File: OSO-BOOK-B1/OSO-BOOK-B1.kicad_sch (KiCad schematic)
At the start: 72 parts, among them J1 USB_C_Receptacle_USB2.0, J2 Conn_01x02_MountingPin, J3 Conn_01x24, J4 Conn_01x06, J5 JST-PH3, J6 JST-PH4, J7 JST-PH3, J8 Conn_ARM_JTAG_SWD_10, Q1 DMG3415, Q2 Q_PMOS_GSD, Q3 Q_NMOS_GSD, U1 XC6220B331MR-G, U2 ESP32-S3-WROOM-1, U3 MEM2075, U4 MCP73831-2-OT, U5 R1218, Y1 32.768 kHz

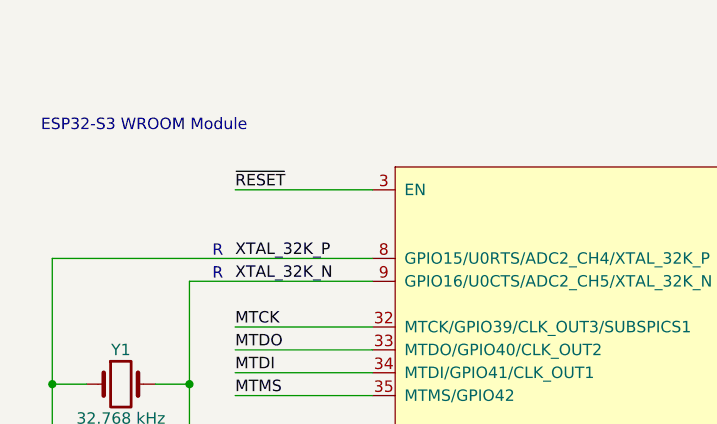
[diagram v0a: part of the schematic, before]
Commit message: add EN pullup to ESP32-S3 book
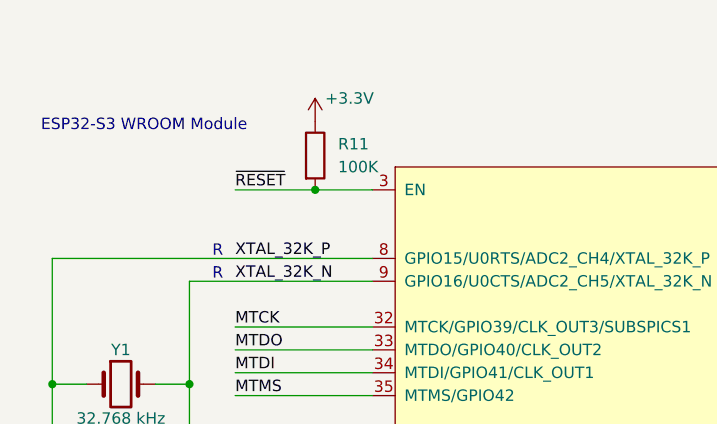
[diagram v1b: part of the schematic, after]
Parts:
- added R11: 100K, Resistor_SMD:R_0805_2012Metric, symbol Device:R
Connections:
- net +3V3: now also R11.1
- net ~{RESET}: now also R11.2
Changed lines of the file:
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@@
   (junction (at 16.51 45.72) (diameter 0) (color 0 0 0 0)
+  )
+  (junction (at 45.72 24.13) (diameter 0) (color 0 0 0 0)
   )
   (junction (at 232.41 149.86) (diameter 0) (color 0 0 0 0)
@@
     (stroke (width 0) (type solid) (color 132 0 0 1))
   )
+  (wire (pts (xy 45.72 24.13) (xy 36.83 24.13))
+    (stroke (width 0) (type default))
+  )
   (wire (pts (xy 44.45 80.01) (xy 36.83 80.01))
     (stroke (width 0) (type default))
@@
     (stroke (width 0) (type default))
   )
-  (wire (pts (xy 52.07 24.13) (xy 36.83 24.13))
+  (wire (pts (xy 52.07 24.13) (xy 45.72 24.13))
     (stroke (width 0) (type default))
   )
@@
     )
   )
+  (symbol (lib_id "Device:R") (at 45.72 20.32 0) (unit 1)
+    (in_bom yes) (on_board yes) (dnp no) (fields_autoplaced)
+    (property "Reference" "R11" (at 48.26 19.0499 0)
+      (effects (font (size 1.27 1.27)) (justify left))
+    )
+    (property "Value" "100K" (at 48.26 21.5899 0)
+      (effects (font (size 1.27 1.27)) (justify left))
+    )
+    (property "Footprint" "Resistor_SMD:R_0805_2012Metric" (at 43.942 20.32 90)
+      (effects (font (size 1.27 1.27)) hide)
+    )
+    (property "Datasheet" "~" (at 45.72 20.32 0)
+      (effects (font (size 1.27 1.27)) hide)
+    )
+    (pin "1")
+    (pin "2")
+    (instances
+      (project "OSO-BOOK-B1"
+        (path "/0e7808ef-4104-4c3a-9f13-425856a8989a"
+          (reference "R11") (unit 1)
+        )
+      )
+      (project "OSO-FLOE-A1"
+        (path "/8cfc6a4c-22f6-4063-b0c4-51ca52a3a57c"
+          (reference "R3") (unit 1)
+        )
+      )
+      (project "OSO-DIGA-A1"
+        (path "/bb4f0314-c44c-4dda-b85c-537120eaae9a"
+          (reference "R4") (unit 1)
+        )
+      )
+    )
+  )
   (symbol (lib_id "Mechanical:Fiducial") (at 262.89 177.8 0) (unit 1)
     (in_bom yes) (on_board yes) (dnp no) (fields_autoplaced)
@@
         )
       )
+    )
+  )
+  (symbol (lib_id "power:+3.3V") (at 45.72 16.51 0) (unit 1)
+    (in_bom yes) (on_board yes) (dnp no)
+    (property "Reference" "#PWR036" (at 45.72 20.32 0)
+      (effects (font (size 1.27 1.27)) hide)
+    )
+    (property "Value" "+3.3V" (at 49.53 13.97 0)
+      (effects (font (size 1.27 1.27)))
+    )
+    (property "Footprint" "" (at 45.72 16.51 0)
+      (effects (font (size 1.27 1.27)) hide)
+    )
+    (property "Datasheet" "" (at 45.72 16.51 0)
+      (effects (font (size 1.27 1.27)) hide)
+    )
+    (pin "1")
+    (instances
+      (project "OSO-BOOK-B1"
+        (path "/0e7808ef-4104-4c3a-9f13-425856a8989a"
+          (reference "#PWR036") (unit 1)
+        )
+      )

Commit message: cleaning up Open Book for Hackaday submission
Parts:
- C19, J4, L2, R8, U5: now not fitted
- C6, C7: value TBD -> 22pF
- Q2: value Q_PMOS_GSD -> DMG3415
- Q3: value Q_NMOS_GSD -> IRLML0100
- RN1: value R_Pack04_Split -> 100K
- Y1: value 32.768 kHz -> 32768 / 12.5pF
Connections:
- net STAT: no longer names the net of U4.1 (STAT)
- no-connect marks 13 -> 14
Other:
- note added: "Battery & Charging"
- note added: "External Power & USB Connection"
- note added: "Power Monitors"
- note added: "STEMMA and STEMMA QT (Extension Ports)"
- note removed: "Battery Monitor"
- note removed: "Power, Battery & USB Connection"
- note removed: "STEMMA and STEMMA QT"
- moved on the sheet: C2, C6, C7, J2, R3, U4

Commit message: fabrication files from hackaday submission, new screen experiment
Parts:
- removed RN1: 100K, Resistor_SMD:R_Array_Concave_4x0603, symbol Device:R_Pack04_Split
- added H5, H6, H7, H8: MountingHole, Tooling_Holes:JLC_Tooling_Hole, symbol Mechanical:MountingHole
- added R12, R13, R14, R15: 100K, Resistor_SMD:R_0805_2012Metric, symbol Device:R
- C19, FID1, FID2, FID3, FID4, H1, H2, H3, H4, J4, JP1, JP2, L2, R8, U5: now left out of the parts list
- L1: value 10µH -> 47µH
- R6: value 0.47 -> 2.2
- R7: now fitted
- U3: footprint MEM2075-00-140-01-A:GCT_MEM2075-00-140-01-A -> New_MicroSD:TF-SMD_TF-PUSH
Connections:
- net +4V: now also R14.1
- net +5V: now also R12.1, R13.1
- net BATMON: now also R14.2, R15.1
- net BUSMON: now also R13.2
- net GND: now also R12.2, R15.2
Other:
- note added: "NOTE: Rev 02 modifies component values to support the GDEY042T81 e-paper display."
- title: The Open Book -> Open Book
- moved on the sheet: H1, H2, H3, H4
